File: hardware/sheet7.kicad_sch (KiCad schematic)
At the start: 7 parts, among them U7 ESP-01

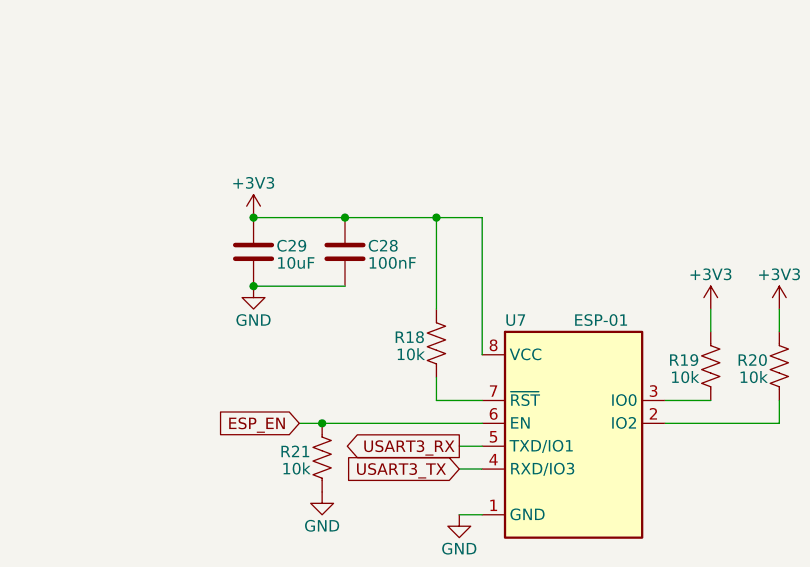
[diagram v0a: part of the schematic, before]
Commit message: hardware(feat): add lcd sheet
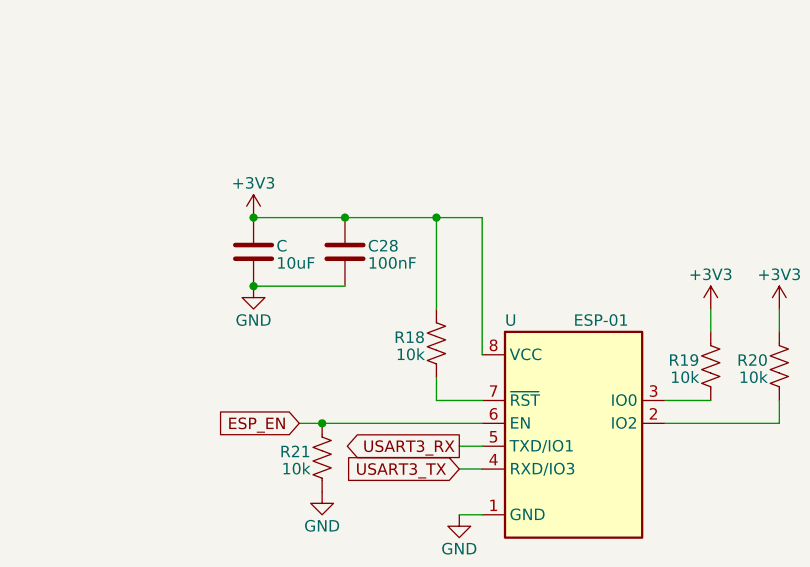
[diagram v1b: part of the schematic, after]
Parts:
- renumbered C29 to C, U7 to U
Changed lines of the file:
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@@
 		(on_board yes)
 		(dnp no)
-		(property "Reference" "U7"
+		(property "Reference" "U"
 			(at 142.24 87.63 0)
 			(effects
@@
 		)
 		(instances
-			(project ""
-				(path "/08767502-fa14-4976-aaca-9650785a2144/4146eae3-5013-424d-958d-e72c053ce55e"
-					(reference "U7")
+			(project "chronolog"
+				(path "/08767502-fa14-4976-aaca-9650785a2144/a2a67f8b-871a-4322-8b22-519f733d7411"
+					(reference "U8")
 					(unit 1)
 				)
@@
 					(unit 1)
 				)
+				(path "/08767502-fa14-4976-aaca-9650785a2144/a2a67f8b-871a-4322-8b22-519f733d7411"
+					(reference "R22")
+					(unit 1)
+				)
 			)
 		)
@@
 					(unit 1)
 				)
+				(path "/08767502-fa14-4976-aaca-9650785a2144/a2a67f8b-871a-4322-8b22-519f733d7411"
+					(reference "C31")
+					(unit 1)
+				)
 			)
 		)
@@
 					(unit 1)
 				)
+				(path "/08767502-fa14-4976-aaca-9650785a2144/a2a67f8b-871a-4322-8b22-519f733d7411"
+					(reference "#PWR066")
+					(unit 1)
+				)
 			)
 		)
@@
 					(unit 1)
 				)
+				(path "/08767502-fa14-4976-aaca-9650785a2144/a2a67f8b-871a-4322-8b22-519f733d7411"
+					(reference "R23")
+					(unit 1)
+				)
 			)
 		)
@@
 		(on_board yes)
 		(dnp no)
-		(property "Reference" "C29"
+		(property "Reference" "C"
 			(at 116.84 79.375 0)
 			(effects
@@
 		)
 		(instances
-			(project ""
-				(path "/08767502-fa14-4976-aaca-9650785a2144/4146eae3-5013-424d-958d-e72c053ce55e"
-					(reference "C29")
+			(project "chronolog"
+				(path "/08767502-fa14-4976-aaca-9650785a2144/a2a67f8b-871a-4322-8b22-519f733d7411"
+					(reference "C30")
 					(unit 1)
 				)
@@
 					(unit 1)
 				)
+				(path "/08767502-fa14-4976-aaca-9650785a2144/a2a67f8b-871a-4322-8b22-519f733d7411"
+					(reference "#PWR065")
+					(unit 1)
+				)
 			)
 		)
@@
 					(unit 1)
 				)
+				(path "/08767502-fa14-4976-aaca-9650785a2144/a2a67f8b-871a-4322-8b22-519f733d7411"
+					(reference "#PWR070")
+					(unit 1)
+				)
 			)
 		)
@@
 					(unit 1)
 				)
+				(path "/08767502-fa14-4976-aaca-9650785a2144/a2a67f8b-871a-4322-8b22-519f733d7411"
+					(reference "R25")
+					(unit 1)
+				)
 			)
 		)
@@
 					(unit 1)
 				)
+				(path "/08767502-fa14-4976-aaca-9650785a2144/a2a67f8b-871a-4322-8b22-519f733d7411"
+					(reference "R24")
+					(unit 1)
+				)
 			)
 		)
@@
 					(unit 1)
 				)
+				(path "/08767502-fa14-4976-aaca-9650785a2144/a2a67f8b-871a-4322-8b22-519f733d7411"
+					(reference "#PWR069")
+					(unit 1)
+				)
 			)
 		)
@@
 					(unit 1)
 				)
+				(path "/08767502-fa14-4976-aaca-9650785a2144/a2a67f8b-871a-4322-8b22-519f733d7411"
+					(reference "#PWR067")
+					(unit 1)
+				)
 			)
 		)
@@
 					(unit 1)
 				)
+				(path "/08767502-fa14-4976-aaca-9650785a2144/a2a67f8b-871a-4322-8b22-519f733d7411"
+					(reference "#PWR068")
+					(unit 1)
+				)

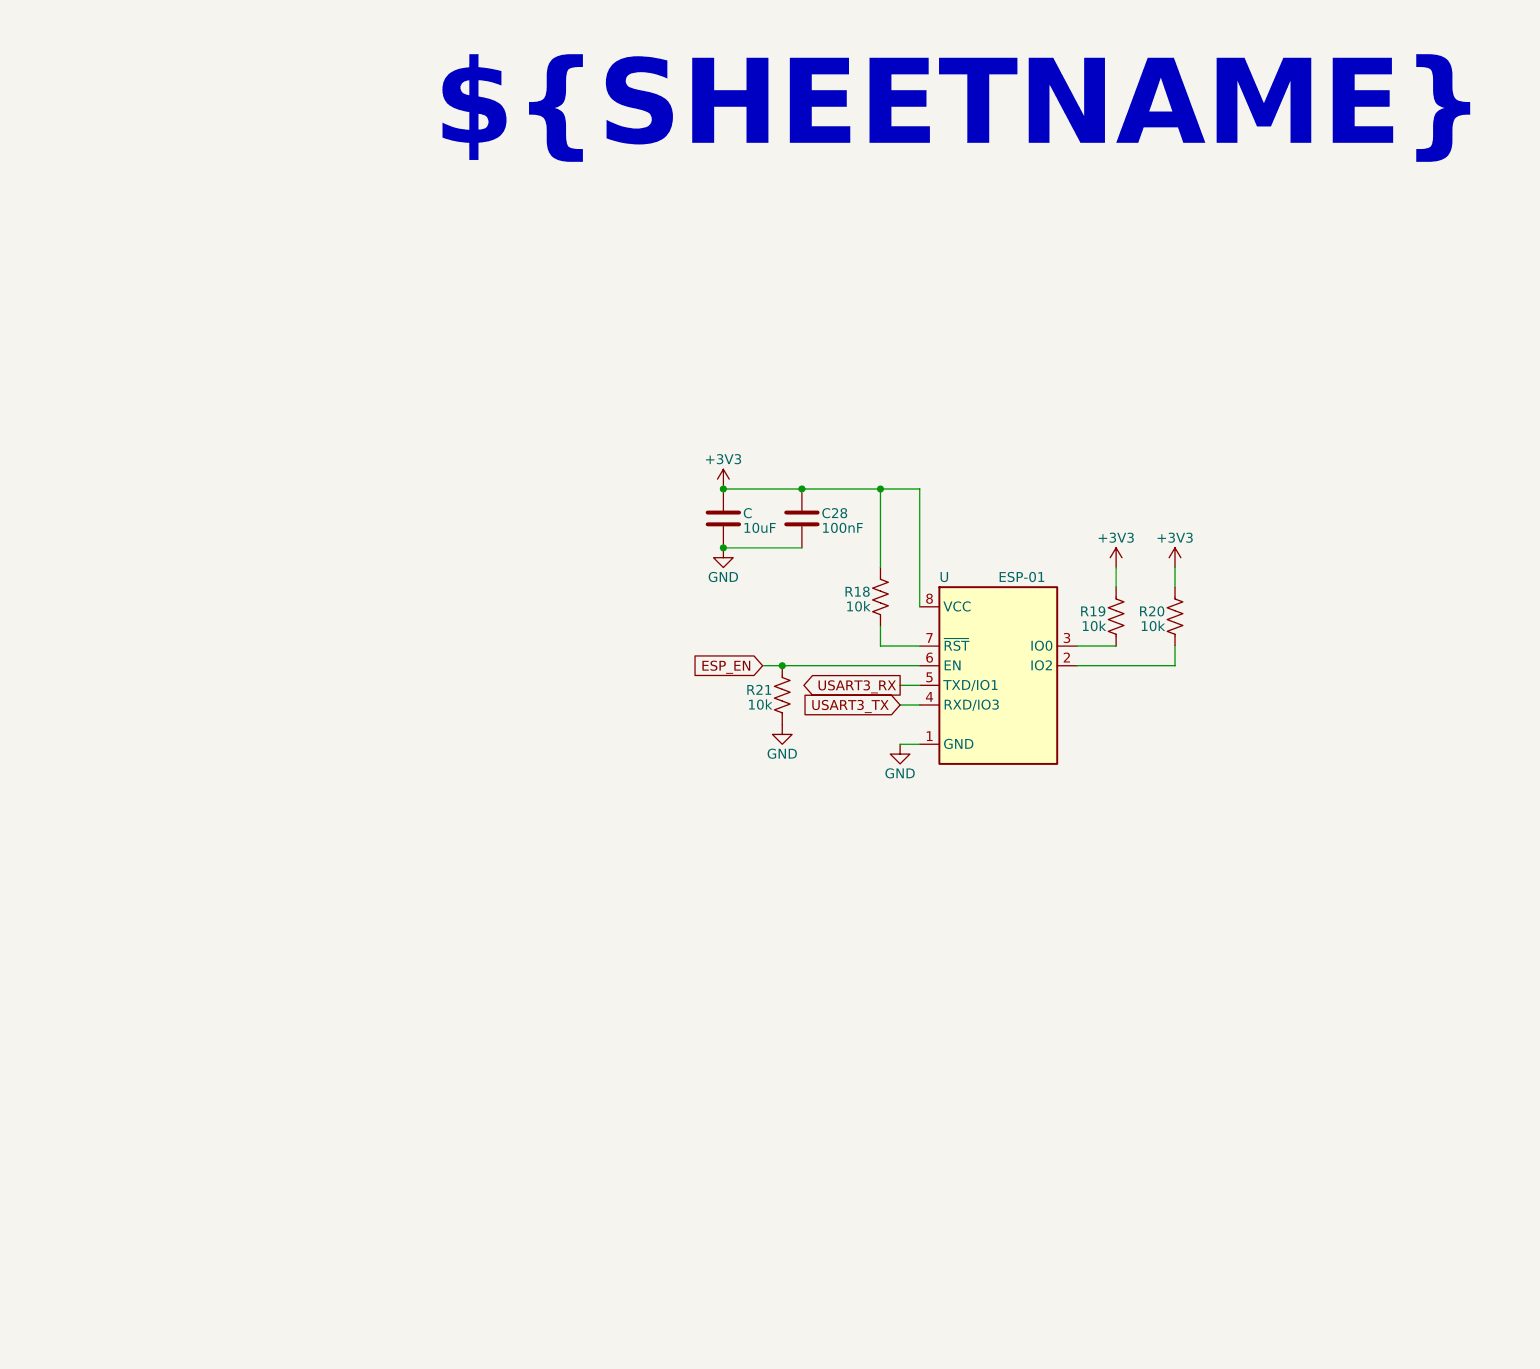
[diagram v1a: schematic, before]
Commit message: hardware(feat): add 16x2 lcd with pcf8574 on i2c1 (#5)
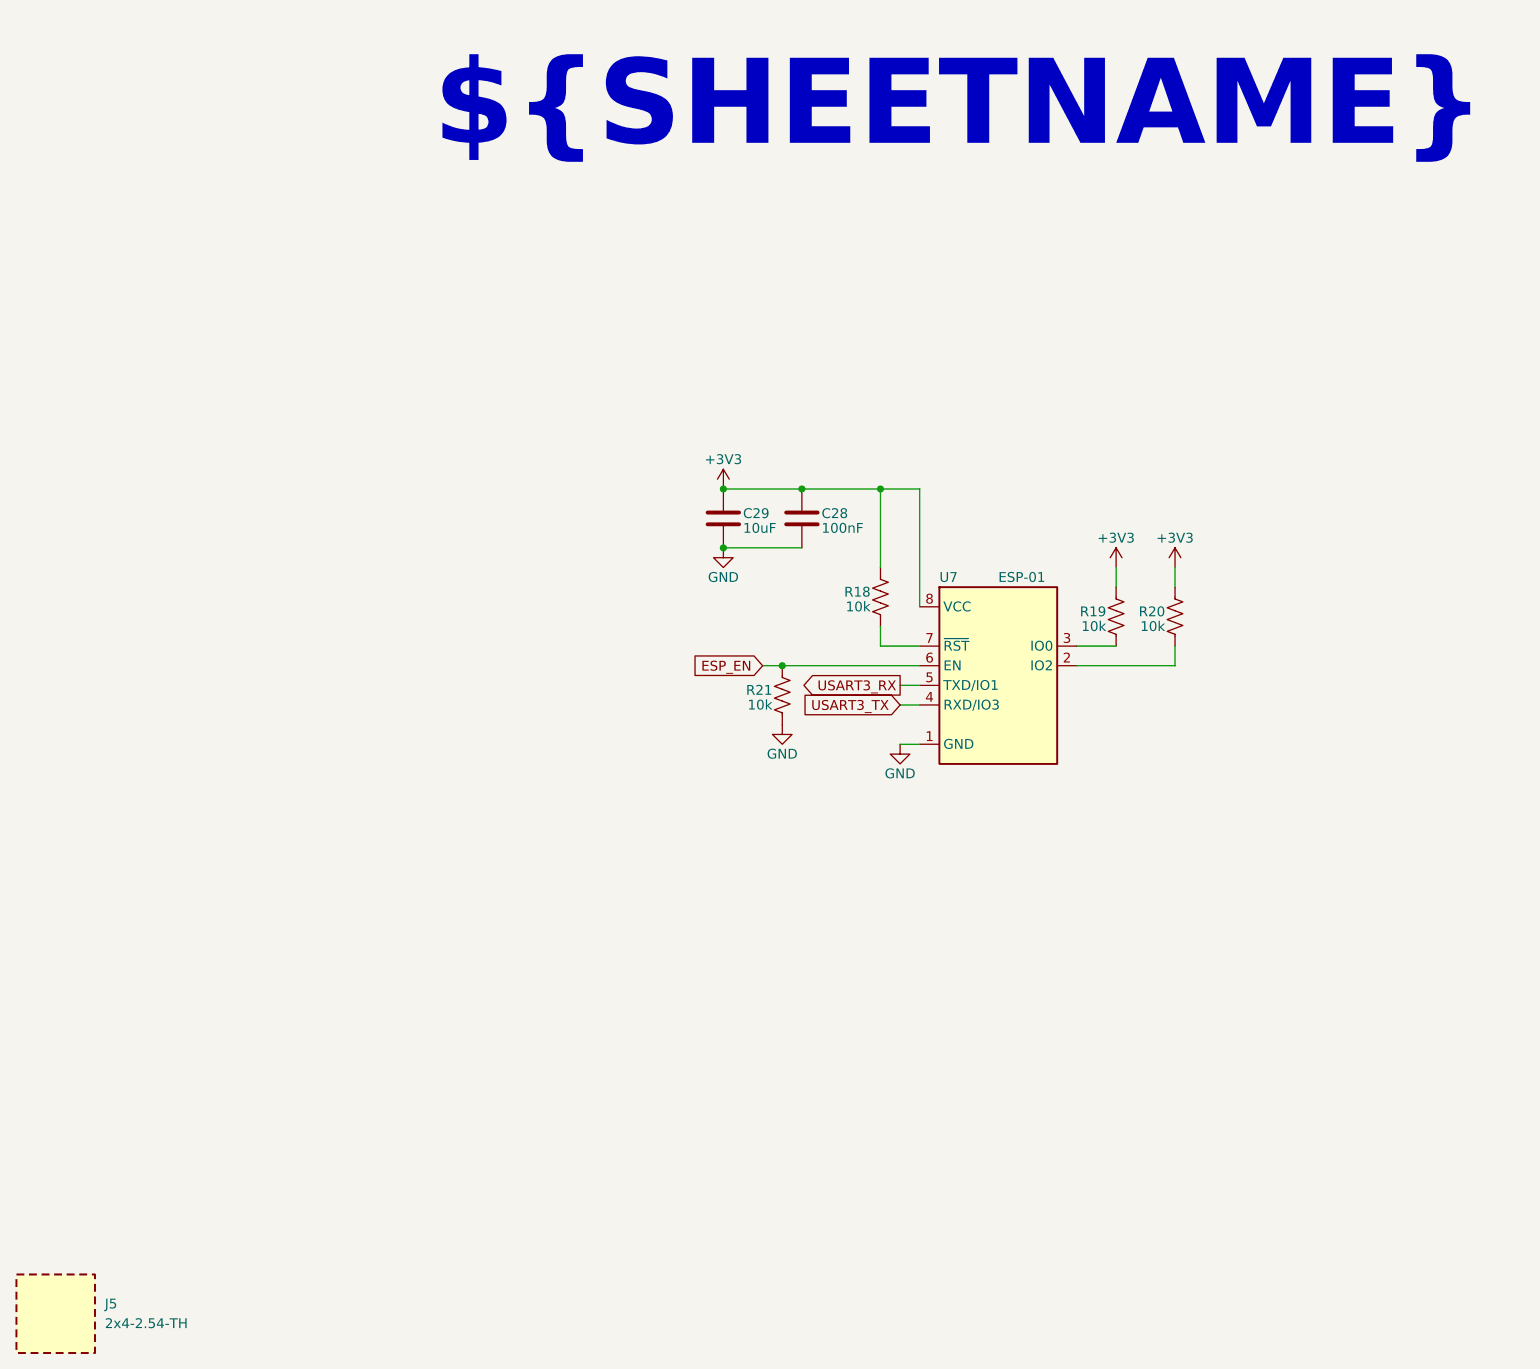
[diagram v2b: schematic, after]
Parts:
- added J5: 2x4-2.54-TH, symbol 08_connectors:CON-SKT_2x4-2.54-TH
- renumbered C to C29, U to U7
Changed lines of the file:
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@@
 		(on_board yes)
 		(dnp no)
-		(property "Reference" "U"
+		(property "Reference" "U7"
 			(at 142.24 87.63 0)
 			(effects
@@
 		)
 		(instances
-			(project "chronolog"
-				(path "/08767502-fa14-4976-aaca-9650785a2144/a2a67f8b-871a-4322-8b22-519f733d7411"
-					(reference "U8")
+			(project ""
+				(path "/08767502-fa14-4976-aaca-9650785a2144/4146eae3-5013-424d-958d-e72c053ce55e"
+					(reference "U7")
 					(unit 1)
 				)
@@
 					(unit 1)
 				)
-				(path "/08767502-fa14-4976-aaca-9650785a2144/a2a67f8b-871a-4322-8b22-519f733d7411"
-					(reference "R22")
-					(unit 1)
-				)
 			)
 		)
@@
 					(unit 1)
 				)
-				(path "/08767502-fa14-4976-aaca-9650785a2144/a2a67f8b-871a-4322-8b22-519f733d7411"
-					(reference "C31")
-					(unit 1)
-				)
 			)
 		)
@@
 					(unit 1)
 				)
-				(path "/08767502-fa14-4976-aaca-9650785a2144/a2a67f8b-871a-4322-8b22-519f733d7411"
-					(reference "#PWR066")
-					(unit 1)
-				)
 			)
 		)
@@
 					(unit 1)
 				)
-				(path "/08767502-fa14-4976-aaca-9650785a2144/a2a67f8b-871a-4322-8b22-519f733d7411"
-					(reference "R23")
-					(unit 1)
-				)
 			)
 		)
@@
 		(on_board yes)
 		(dnp no)
-		(property "Reference" "C"
+		(property "Reference" "C29"
 			(at 116.84 79.375 0)
 			(effects
@@
 		)
 		(instances
-			(project "chronolog"
-				(path "/08767502-fa14-4976-aaca-9650785a2144/a2a67f8b-871a-4322-8b22-519f733d7411"
-					(reference "C30")
+			(project ""
+				(path "/08767502-fa14-4976-aaca-9650785a2144/4146eae3-5013-424d-958d-e72c053ce55e"
+					(reference "C29")
 					(unit 1)
 				)
@@
 					(unit 1)
 				)
-				(path "/08767502-fa14-4976-aaca-9650785a2144/a2a67f8b-871a-4322-8b22-519f733d7411"
-					(reference "#PWR065")
-					(unit 1)
-				)
 			)
 		)
@@
 					(unit 1)
 				)
-				(path "/08767502-fa14-4976-aaca-9650785a2144/a2a67f8b-871a-4322-8b22-519f733d7411"
-					(reference "#PWR070")
-					(unit 1)
-				)
 			)
 		)
@@
 					(unit 1)
 				)
-				(path "/08767502-fa14-4976-aaca-9650785a2144/a2a67f8b-871a-4322-8b22-519f733d7411"
-					(reference "R25")
-					(unit 1)
-				)
 			)
 		)
@@
 					(unit 1)
 				)
-				(path "/08767502-fa14-4976-aaca-9650785a2144/a2a67f8b-871a-4322-8b22-519f733d7411"
-					(reference "R24")
-					(unit 1)
-				)
 			)
 		)
@@
 					(unit 1)
 				)
-				(path "/08767502-fa14-4976-aaca-9650785a2144/a2a67f8b-871a-4322-8b22-519f733d7411"
-					(reference "#PWR069")
-					(unit 1)
-				)
 			)
 		)
@@
 					(unit 1)
 				)
-				(path "/08767502-fa14-4976-aaca-9650785a2144/a2a67f8b-871a-4322-8b22-519f733d7411"
-					(reference "#PWR067")
+			)
+		)
+	)
+	(symbol
+		(lib_id "08_connectors:CON-SKT_2x4-2.54-TH")
+		(at 27.94 182.88 0)
+		(unit 1)
+		(exclude_from_sim no)
+		(in_bom yes)
+		(on_board no)
+		(dnp no)
+		(fields_autoplaced yes)
+		(property "Reference" "J5"
+			(at 34.29 181.6099 0)
+			(effects
+				(font
+					(size 1.27 1.27)
+				)
+				(justify left)
+			)
+		)
+		(property "Value" "2x4-2.54-TH"
+			(at 34.29 184.1499 0)
+			(effects
+				(font
+					(size 1.27 1.27)
+				)
+				(justify left)
+			)
+		)
+		(property "Footprint" ""
+			(at 27.94 182.88 0)
+			(effects
+				(font
+					(size 1.27 1.27)
+				)
+				(hide yes)
+			)
+		)
+		(property "Datasheet" "https://www.lcsc.com/product-detail/C2897405.html"
+			(at 27.94 182.88 0)
+			(effects
+				(font
+					(size 1.27 1.27)
+				)
+				(hide yes)
+			)
+		)
+		(property "Description" "Female header 2x4 2.54mm pitch through hole 8.5mm insulator, board side receptacle for an ESP-01 module, no footprint of its own, its pads belong to 11_modules:ESP-01"
+			(at 27.94 182.88 0)
+			(effects
+				(font
+					(size 1.27 1.27)
+				)
+				(hide yes)
+			)
+		)
+		(property "Package" "TH"
+			(at 27.94 182.88 0)
+			(effects
+				(font
+					(size 1.27 1.27)
+				)
+				(hide yes)
+			)
+		)
+		(property "Manufacturer" "HCTL"
+			(at 27.94 182.88 0)
+			(effects
+				(font
+					(size 1.27 1.27)
+				)
+				(hide yes)
+			)
+		)
+		(property "MPN" "PM254-2-04-Z-8.5"
+			(at 27.94 182.88 0)
+			(effects
+				(font
+					(size 1.27 1.27)
+				)
+				(hide yes)
+			)
+		)
+		(property "LCSC" "C2897405"
+			(at 27.94 182.88 0)
+			(effects
+				(font
+					(size 1.27 1.27)
+				)
+				(hide yes)
+			)
+		)
+		(property "Mates_With" "11_modules:ESP-01"
+			(at 27.94 182.88 0)
+			(effects
+				(font
+					(size 1.27 1.27)
+				)
+				(hide yes)
+			)
+		)
+		(instances
+			(project ""
+				(path "/08767502-fa14-4976-aaca-9650785a2144/4146eae3-5013-424d-958d-e72c053ce55e"
+					(reference "J5")
 					(unit 1)
 				)
@@
 					(unit 1)
 				)
-				(path "/08767502-fa14-4976-aaca-9650785a2144/a2a67f8b-871a-4322-8b22-519f733d7411"
-					(reference "#PWR068")
-					(unit 1)
-				)
